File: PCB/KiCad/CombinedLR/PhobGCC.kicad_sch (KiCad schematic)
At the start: 80 parts, among them J1 Conn_01x06_Female, J2 Conn_01x04_Female, J3 Conn_01x01_Male, J4 Conn_01x04_Male, J5 Rumble, J6 L, J7 R, Q1 Q_NMOS_GSD, Q2 Q_PMOS_GDS, Q3 Q_NMOS_GSD, SW1 A, SW10 Dup, SW11 Dright, SW12 Ddown, SW13 L, SW14 R, SW2 B, SW3 X, SW4 Y, SW5 Start, SW6 L, SW7 R, SW8 Z, SW9 Dleft, U1 Teensy4.0, U2 2x DRV5053CAQLPGM Hall Effect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, U3 GP2S60-MFG, U4 GP2S60-MFG, U5 Stickbox_Assembly

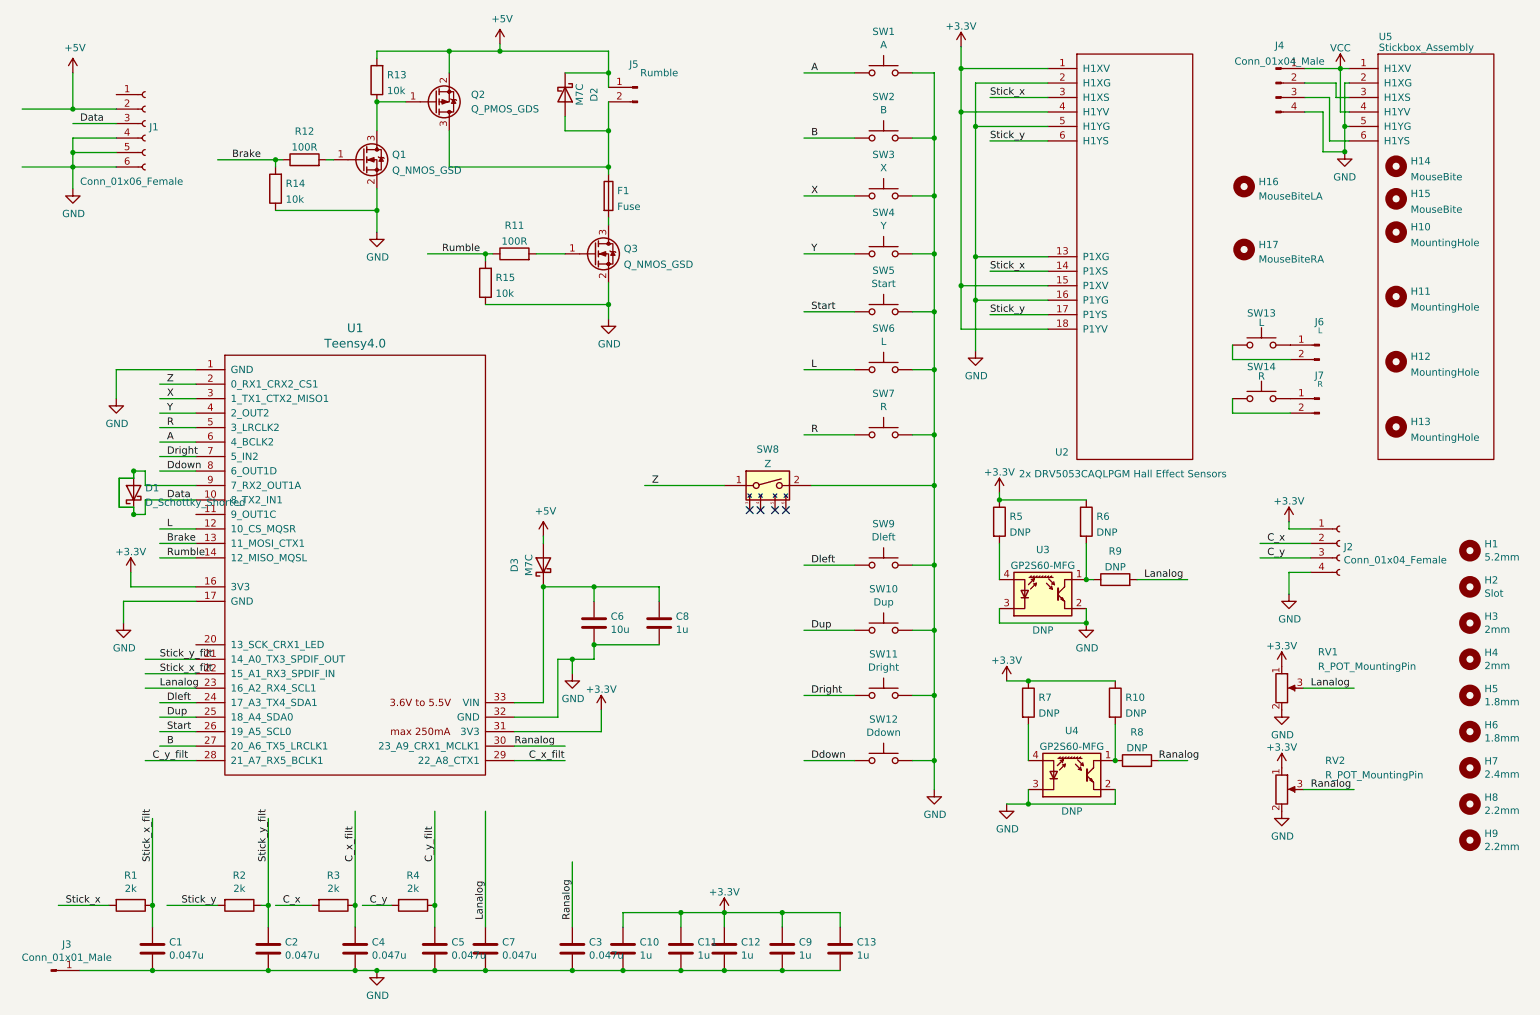
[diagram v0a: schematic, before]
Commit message: Separating schematic into multiple sheets
Locked GameCube-specific PCB components (stickboxes, sliders, etc.). Created separate schematic sheets to more easily track and identify changes.
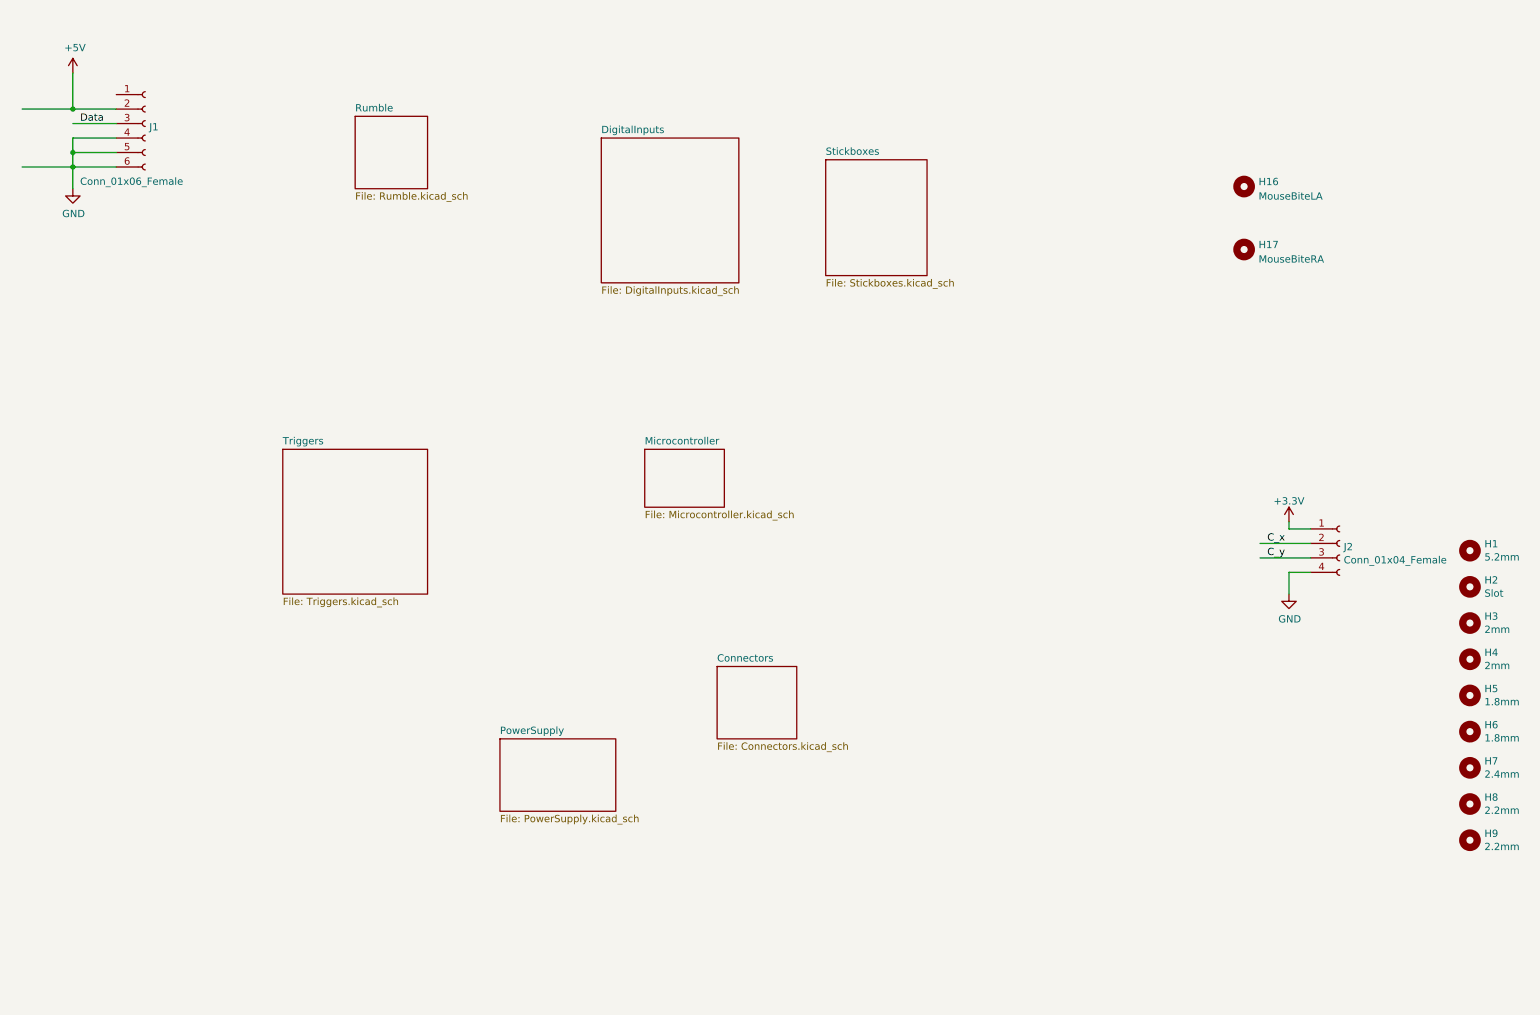
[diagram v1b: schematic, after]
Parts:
- removed C1, C2, C3, C4, C5, C7: 0.047u, PhobGCC_Footprints:C_0603_HandSoldering, symbol Device:C
- removed C10, C11, C12, C13, C8, C9: 1u, PhobGCC_Footprints:C_0603_1608Metric_Pad1.08x0.95mm_HandSolder, symbol Device:C
- removed C6: 10u, PhobGCC_Footprints:C_0603_HandSoldering, symbol Device:C
- removed D1: D_Schottky_Shorted, PhobGCC_Footprints:D_SOD-523_Shorted, symbol PhobGCC_Symbol_Library:D_Schottky_Shorted
- removed D2, D3: M7C, PhobGCC_Footprints:D_SOD-123, symbol Device:D_Schottky
- removed F1: Fuse, PhobGCC_Footprints:Fuse_1206_3216Metric, symbol Device:Fuse
- removed H10: MountingHole, PhobGCC_Footprints:MountingHole_1.8mm, symbol Mechanical:MountingHole
- removed H11: MountingHole, PhobGCC_Footprints:MountingHole_5.2mm, symbol Mechanical:MountingHole
- removed H12, H13: MountingHole, PhobGCC_Footprints:MountingHole_2.0mm, symbol Mechanical:MountingHole
- removed H14, H15: MouseBite, PhobGCC_Footprints:breakaway-mousebites-double, symbol Mechanical:MountingHole
- removed J3: Conn_01x01_Male, PhobGCC_Footprints:PinHeader_1x01_P2.54mm_Vertical, symbol Connector:Conn_01x01_Male
- removed J4: Conn_01x04_Male, PhobGCC_Footprints:PinHeader_1x04_P2.00mm_Vertical, symbol Connector:Conn_01x04_Male
- removed J5: Rumble, PhobGCC_Footprints:rumble_pins, symbol Connector:Conn_01x02_Male
- removed J6: L, PhobGCC_Footprints:Pin_Header_Straight_1x02_Pitch2.54mm, symbol Connector:Conn_01x02_Male
- removed J7: R, PhobGCC_Footprints:Pin_Header_Straight_1x02_Pitch2.54mm, symbol Connector:Conn_01x02_Male
- removed Q1, Q3: Q_NMOS_GSD, PhobGCC_Footprints:SOT-23, symbol Device:Q_NMOS_GSD
- removed Q2: Q_PMOS_GDS, PhobGCC_Footprints:SOT-23, symbol Device:Q_PMOS_GSD
- removed R1, R2, R3, R4: 2k, PhobGCC_Footprints:R_0603_1608Metric_Pad0.98x0.95mm_HandSolder, symbol Device:R
- removed R10, R5, R6, R7, R8, R9: DNP, PhobGCC_Footprints:R_0603_1608_DNP, symbol Device:R
- removed R11, R12: 100R, PhobGCC_Footprints:R_0603_1608Metric_Pad0.98x0.95mm_HandSolder, symbol Device:R
- removed R13, R14, R15: 10k, PhobGCC_Footprints:R_0603_1608Metric_Pad0.98x0.95mm_HandSolder, symbol Device:R
- removed RV1, RV2: R_POT_MountingPin, PhobGCC_Footprints:GCC_Slider, symbol GCC:Gamecube-MB-rescue_Slider_GCC-Gamecube_MB
- removed SW1: A, PhobGCC_Footprints:ABXY_Contact_Omron_Switch, symbol Switch:SW_Push
- removed SW10: Dup, PhobGCC_Footprints:Dpad_Contact_TL3315NF_2, symbol Switch:SW_Push
- removed SW11: Dright, PhobGCC_Footprints:Dpad_Contact_TL3315NF_2, symbol Switch:SW_Push
- removed SW12: Ddown, PhobGCC_Footprints:Dpad_Contact_TL3315NF_2, symbol Switch:SW_Push
- removed SW13: L, PhobGCC_Footprints:Trigger_Contact, symbol Switch:SW_Push
- removed SW14: R, PhobGCC_Footprints:Trigger_Contact, symbol Switch:SW_Push
- removed SW2: B, PhobGCC_Footprints:ABXY_Contact_Omron_Switch, symbol Switch:SW_Push
- removed SW3: X, PhobGCC_Footprints:ABXY_Contact_Omron_Switch, symbol Switch:SW_Push
- removed SW4: Y, PhobGCC_Footprints:ABXY_Contact_Omron_Switch, symbol Switch:SW_Push
- removed SW5: Start, PhobGCC_Footprints:Start_Contact, symbol Switch:SW_Push
- removed SW6: L, PhobGCC_Footprints:Pin_Header_Straight_1x02_Pitch2.54mm, symbol Switch:SW_Push
- removed SW7: R, PhobGCC_Footprints:Pin_Header_Straight_1x02_Pitch2.54mm, symbol Switch:SW_Push
- removed SW8: Z, symbol PhobGCC_Symbol_Library:SW_DIP_x01
- removed SW9: Dleft, PhobGCC_Footprints:Dpad_Contact_TL3315NF_2, symbol Switch:SW_Push
- removed U1: Teensy4.0, PhobGCC_Footprints:Teensy40_Edge_Pins, symbol teensy:Teensy4.0
- removed U2: 2x DRV5053CAQLPGM Hall Effect Sensors, PhobGCC_Footprints:GCC_Stickbox_2, symbol GCC:Gamecube-MB-rescue_Stickbox_Assembly-Gamecube_MB
- removed U3, U4: GP2S60-MFG, PhobGCC_Footprints:Sharp_Microelectronics-GP2S60-MFG, symbol Sensor_Proximity:BPR-105
- removed U5: Stickbox_Assembly, PhobGCC_Footprints:GCC_Stickbox_Hall_Only, symbol Gamecube MB:Stickbox_Assembly_Hall_Only
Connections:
- no-connect marks 4 -> 0
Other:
- added sheet Connectors (Connectors.kicad_sch)
- added sheet DigitalInputs (DigitalInputs.kicad_sch)
- added sheet Microcontroller (Microcontroller.kicad_sch)
- added sheet PowerSupply (PowerSupply.kicad_sch)
- added sheet Rumble (Rumble.kicad_sch)
- added sheet Stickboxes (Stickboxes.kicad_sch)
- added sheet Triggers (Triggers.kicad_sch)
